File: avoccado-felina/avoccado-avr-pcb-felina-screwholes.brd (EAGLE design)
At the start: 44 x 17.5 mm, 79 parts, among them Q1 16MHz, Q2 FET, U1 MPU-6000QFN-24, U2 MCP73831

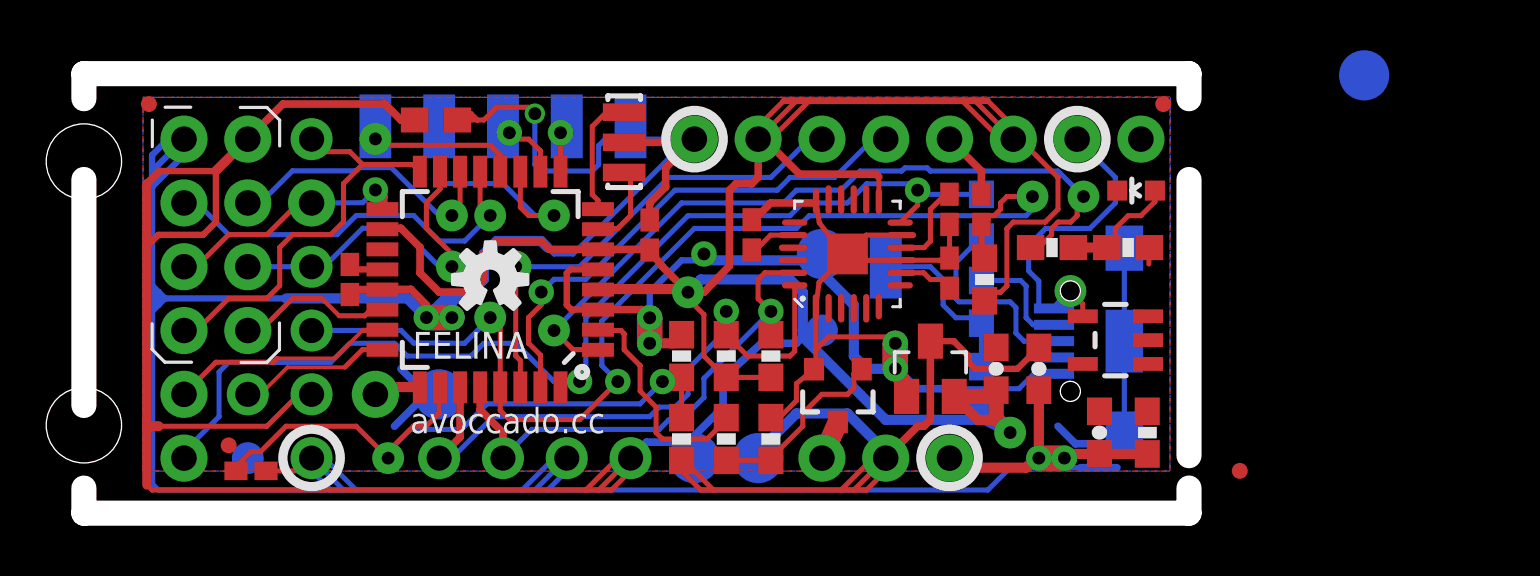
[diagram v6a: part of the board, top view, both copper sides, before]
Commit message: no airwires left, added 5V USB power LED
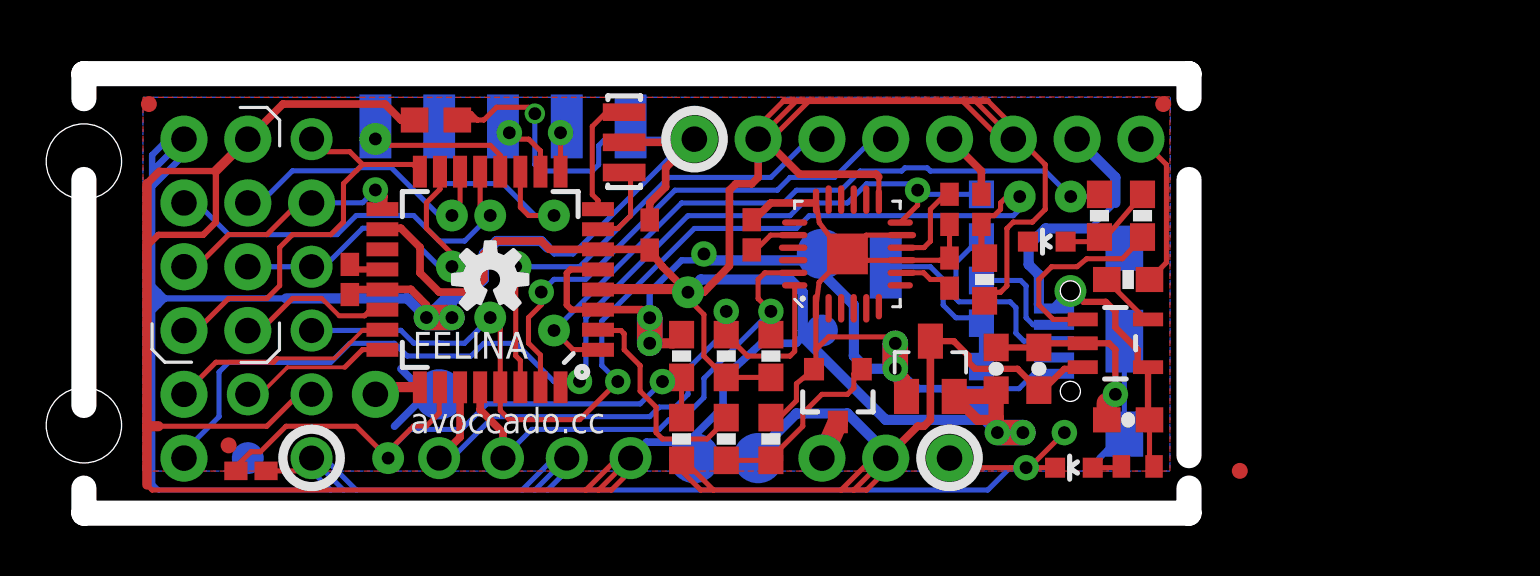
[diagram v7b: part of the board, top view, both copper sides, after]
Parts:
- removed TP14: TPTP20R, testpad:TP20R
- added D2: LED, SparkFun:LED-0603
- added R9: 2K, rcl:R0402
- moved R3 6.14 mm to (42.7, 32.5), turned to 180 degrees
- moved D1 4.10 mm to (39.4, 34.0)
- moved R6 2.28 mm to (41.5, 35.1), turned to 270 degrees
- moved R4 1.39 mm to (43.2, 35.1), turned to 270 degrees
- moved C4 1.25 mm to (42.7, 26.9), turned to 180 degrees
- moved U2 0.13 mm to (42.2, 30.0), turned to 270 degrees
- turned C5 to 90 degrees
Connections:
- new net N$3: D2.A, R9.1
- net 5V: now also R9.2; no longer TP14.TP
- net GND: now also D2.C
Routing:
- net 5V: track 12.8 -> 20.7 mm
- net SOC: track 0.66 -> 7.83 mm
- net CHG-PROG: track 0.00 -> 2.44 mm
- net D3: track 29.7 -> 27.3 mm
- net VBAT: track 33.0 -> 35.2 mm
- net GND: track 211.1 -> 212.7 mm, vias 10 -> 11
- net N$3: track 0.00 -> 1.16 mm
- net RESET: track 43.3 -> 42.2 mm
- net 3.3V: track 166.9 -> 167.2 mm, vias 2 -> 3
